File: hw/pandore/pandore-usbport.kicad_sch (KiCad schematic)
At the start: 12 parts, among them J2 USB2-A_2stacked, J3 USB3-A_2stacked

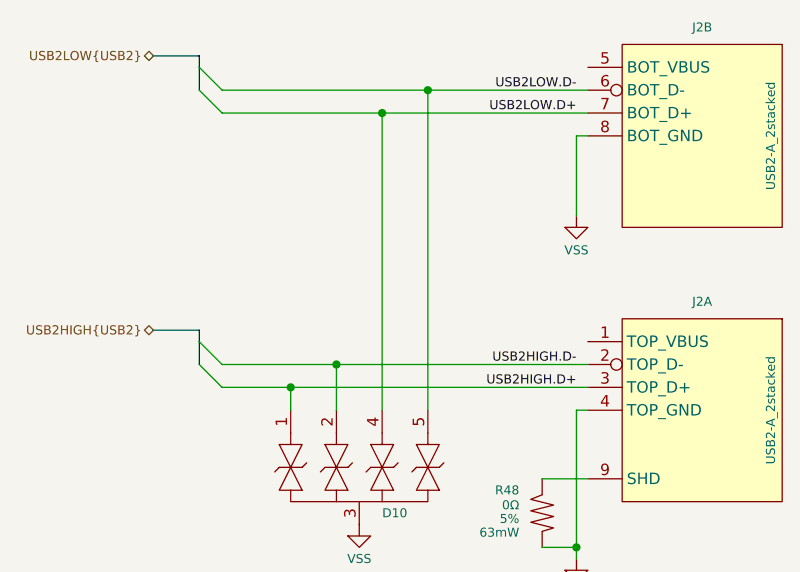
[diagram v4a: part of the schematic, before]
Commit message: added encoder, more routing done, pinout doc added
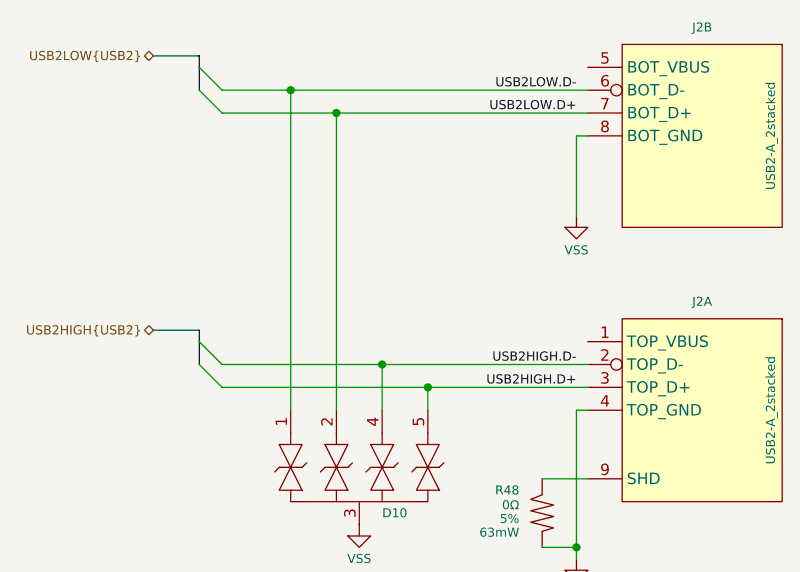
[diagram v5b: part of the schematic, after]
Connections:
- net USB2HIGH.D+: now also D10.5; no longer D10.1
- net USB2HIGH.D-: now also D10.4; no longer D10.2
- net USB2LOW.D+: now also D10.2; no longer D10.4
- net USB2LOW.D-: now also D10.1; no longer D10.5
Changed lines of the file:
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@@
-	)
-	(junction
-		(at 226.06 52.07)
-		(diameter 0)
-		(color 0 0 0 0)
 	)
 	(junction
@@
 	)
 	(junction
-		(at 231.14 24.13)
+		(at 226.06 24.13)
 		(diameter 0)
 		(color 0 0 0 0)
@@
 	)
 	(junction
+		(at 231.14 52.07)
+		(diameter 0)
+		(color 0 0 0 0)
+	)
+	(junction
 		(at 218.44 113.03)
 		(diameter 0)
@@
 	)
 	(junction
+		(at 220.98 21.59)
+		(diameter 0)
+		(color 0 0 0 0)
+	)
+	(junction
 		(at 223.52 110.49)
 		(diameter 0)
@@
 	)
 	(junction
+		(at 236.22 54.61)
+		(diameter 0)
+		(color 0 0 0 0)
+	)
+	(junction
 		(at 222.25 160.02)
 		(diameter 0)
@@
 	)
 	(junction
-		(at 236.22 21.59)
-		(diameter 0)
-		(color 0 0 0 0)
-	)
-	(junction
-		(at 220.98 54.61)
-		(diameter 0)
-		(color 0 0 0 0)
-	)
-	(junction
 		(at 210.82 95.25)
 		(diameter 0)
@@
 	(wire
 		(pts
+			(xy 231.14 52.07) (xy 231.14 57.15)
+		)
+		(stroke
+			(width 0)
+			(type default)
+		)
+	)
+	(wire
+		(pts
+			(xy 236.22 54.61) (xy 236.22 57.15)
+		)
+		(stroke
+			(width 0)
+			(type default)
+		)
+	)
+	(wire
+		(pts
 			(xy 176.53 110.49) (xy 190.5 110.49)
 		)
@@
 	(wire
 		(pts
-			(xy 213.36 54.61) (xy 220.98 54.61)
+			(xy 213.36 54.61) (xy 236.22 54.61)
 		)
 		(stroke
@@
 	(wire
 		(pts
+			(xy 226.06 24.13) (xy 254 24.13)
+		)
+		(stroke
+			(width 0)
+			(type default)
+		)
+	)
+	(wire
+		(pts
+			(xy 231.14 52.07) (xy 254 52.07)
+		)
+		(stroke
+			(width 0)
+			(type default)
+		)
+	)
+	(wire
+		(pts
 			(xy 248.92 64.77) (xy 254 64.77)
 		)
@@
 	(wire
 		(pts
-			(xy 220.98 54.61) (xy 254 54.61)
-		)
-		(stroke
-			(width 0)
-			(type default)
-		)
-	)
-	(wire
-		(pts
 			(xy 176.53 160.02) (xy 190.5 160.02)
 		)
@@
 	(wire
 		(pts
-			(xy 226.06 52.07) (xy 254 52.07)
-		)
-		(stroke
-			(width 0)
-			(type default)
-		)
-	)
-	(wire
-		(pts
-			(xy 236.22 21.59) (xy 236.22 57.15)
+			(xy 213.36 52.07) (xy 231.14 52.07)
 		)
 		(stroke
@@
 	(wire
 		(pts
-			(xy 213.36 21.59) (xy 236.22 21.59)
+			(xy 213.36 21.59) (xy 220.98 21.59)
 		)
 		(stroke
@@
 	(wire
 		(pts
-			(xy 213.36 52.07) (xy 226.06 52.07)
-		)
-		(stroke
-			(width 0)
-			(type default)
-		)
-	)
-	(wire
-		(pts
 			(xy 232.41 152.4) (xy 232.41 165.1)
 		)
@@
 	(wire
 		(pts
-			(xy 231.14 24.13) (xy 231.14 57.15)
-		)
-		(stroke
-			(width 0)
-			(type default)
-		)
-	)
-	(wire
-		(pts
 			(xy 227.33 154.94) (xy 254 154.94)
 		)
@@
 	(wire
 		(pts
+			(xy 236.22 54.61) (xy 254 54.61)
+		)
+		(stroke
+			(width 0)
+			(type default)
+		)
+	)
+	(wire
+		(pts
 			(xy 252.73 72.39) (xy 252.73 57.15)
 		)
@@
 	(wire
 		(pts
-			(xy 231.14 24.13) (xy 254 24.13)
-		)
-		(stroke
-			(width 0)
-			(type default)
-		)
-	)
-	(wire
-		(pts
 			(xy 254 97.79) (xy 252.73 97.79)
 		)
@@
 		)
 	)
-	(wire
-		(pts
-			(xy 220.98 54.61) (xy 220.98 57.15)
-		)
-		(stroke
-			(width 0)
-			(type default)
-		)
-	)
 	(bus
 		(pts
@@
 		)
 	)
+	(wire
+		(pts
+			(xy 220.98 21.59) (xy 220.98 57.15)
+		)
+		(stroke
+			(width 0)
+			(type default)
+		)
+	)
 	(bus
 		(pts
@@
 	(wire
 		(pts
+			(xy 226.06 24.13) (xy 226.06 57.15)
+		)
+		(stroke
+			(width 0)
+			(type default)
+		)
+	)
+	(wire
+		(pts
 			(xy 252.73 57.15) (xy 254 57.15)
 		)
@@
 	(wire
 		(pts
-			(xy 226.06 52.07) (xy 226.06 57.15)
-		)
-		(stroke
-			(width 0)
-			(type default)
-		)
-	)
-	(wire
-		(pts
 			(xy 176.53 92.71) (xy 208.28 92.71)
 		)
@@
 	(wire
 		(pts
-			(xy 236.22 21.59) (xy 254 21.59)
+			(xy 220.98 21.59) (xy 254 21.59)
 		)
 		(stroke
@@
 	(wire
 		(pts
-			(xy 213.36 24.13) (xy 231.14 24.13)
-		)
-		(stroke
+			(xy 213.36 24.13) (xy 226.06 24.13)
+		)
+		(stroke

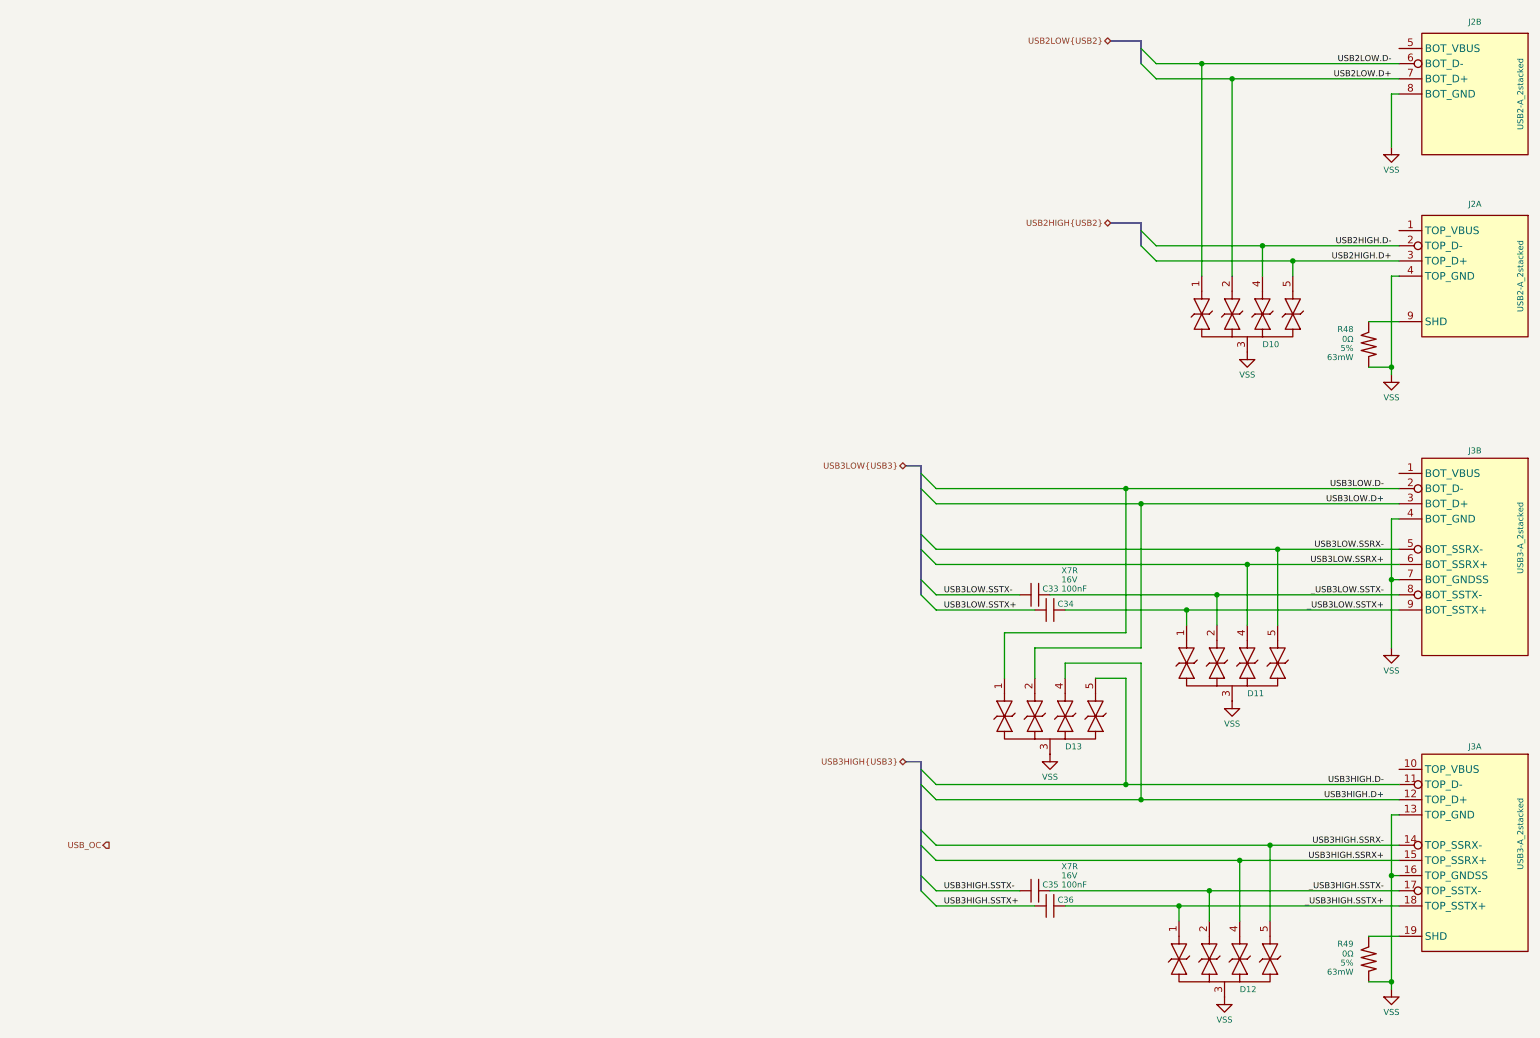
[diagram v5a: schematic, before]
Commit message: lcd control circuit added fan interface added rgba output pinout for management mcu accessories done
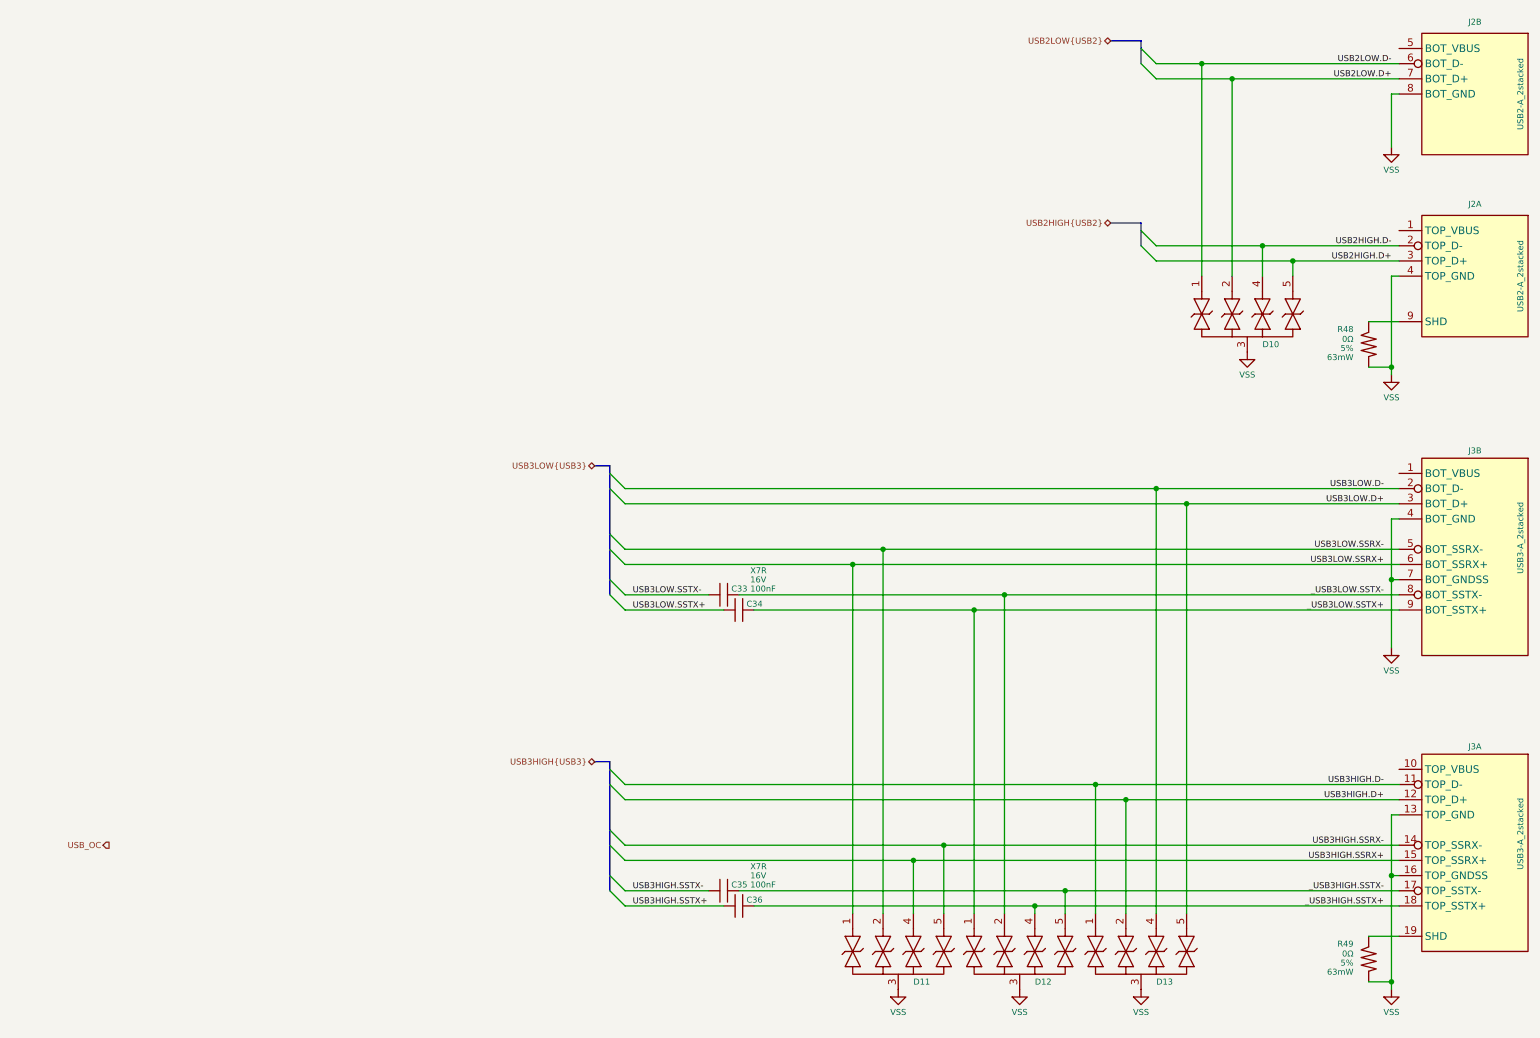
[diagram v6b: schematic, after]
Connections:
- net USB3HIGH.D+: now also D13.2; no longer D13.4
- net USB3HIGH.D-: now also D13.1; no longer D13.5
- net USB3HIGH.SSRX+: now also D11.4; no longer D12.4
- net USB3HIGH.SSRX-: now also D11.5; no longer D12.5
- net USB3LOW.D+: now also D13.5; no longer D13.2
- net USB3LOW.D-: now also D13.4; no longer D13.1
- net USB3LOW.SSRX+: now also D11.1; no longer D11.4
- net USB3LOW.SSRX-: now also D11.2; no longer D11.5
- net _USB3HIGH.SSTX+: now also D12.4; no longer D12.1
- net _USB3HIGH.SSTX-: now also D12.5; no longer D12.2
- net _USB3LOW.SSTX+: now also D12.1; no longer D11.1
- net _USB3LOW.SSTX-: now also D12.2; no longer D11.2
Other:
- moved on the sheet: C33, C34, C35, C36, D11, D12, D13

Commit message: more routing/placement done added 5v load switch 1A each added second fan circuit redone all diffpair routing following new stackup calc added all (?) missing connectors to unused pins
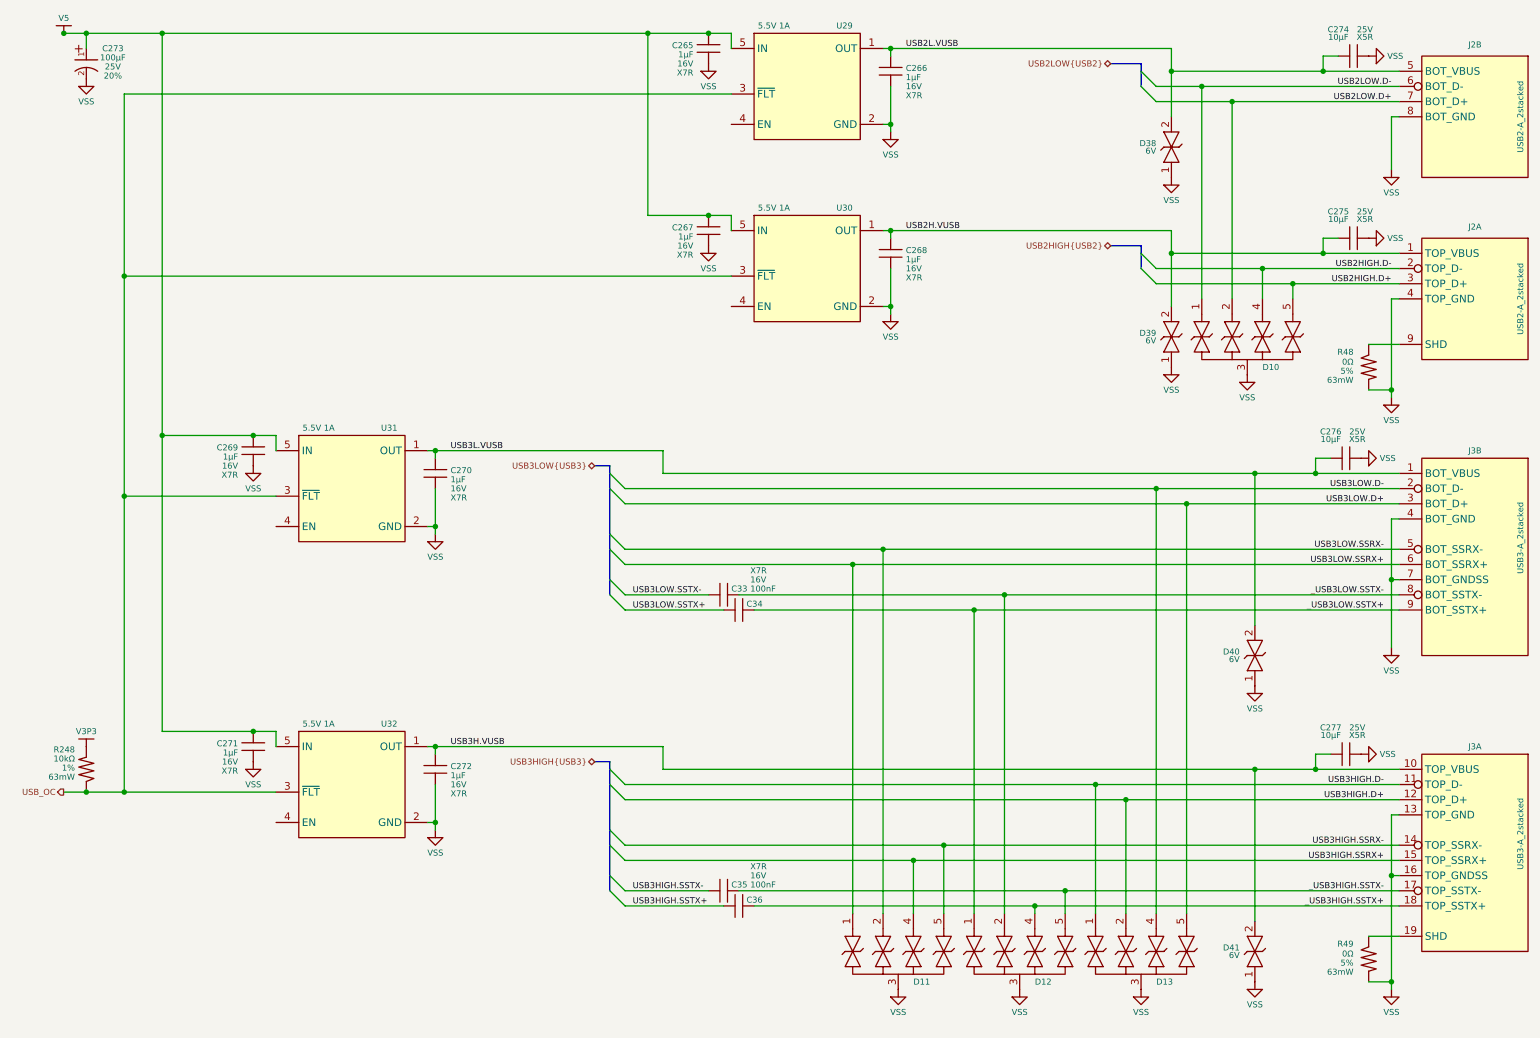
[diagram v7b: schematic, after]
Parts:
- added C265, C266, C267, C268, C269, C270, C271, C272: ${Capacitance}, ${Voltage}, ${Dielectric}, reekilib_cap:CAPC1608, symbol reekilib_cap:cap
- added C273: ${Capacitance}, ${Voltage}, ${Tolerance}, reekilib_cap:CAPAE630Xxxx, symbol reekilib_cap:cap_pol
- added C274, C275, C276, C277: ${Capacitance}, ${Voltage}, ${Dielectric}, reekilib_cap:CAPC2012, symbol reekilib_cap:cap
- added D38, D39, D40, D41: 6V, reekilib_dio:dio_sma, symbol reekilib_tvs:diode_tvsbi
- added R248: ${Resistance}, ${Tolerance}, ${Power}, reekilib_res:RESC1005, symbol reekilib_res:res
- added U29, U30, U31, U32: 5.5V 1A, reekilib_sot:SOT95P280X100-5, symbol reekilib_psw:ET2016x
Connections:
- net USB_OC: now also R248.2, U29.3 (~{FLT}), U30.3 (~{FLT}), U31.3 (~{FLT}), U32.3 (~{FLT})
- net VSS: now also C265.1, C266.1, C267.1, C268.1, C269.1, C270.1, C271.1, C272.1, C273.2 (-), C274.1, C275.1, C276.1, C277.1, D38.1, D39.1, D40.1, D41.1, U29.2 (GND), U30.2 (GND), U31.2 (GND), U32.2 (GND)
- net USB3L.VUSB: now reaches J3.1 (BOT_VBUS)
- net USB3L.VUSB: now also C270.2, C276.2, D40.2, U31.1 (OUT)
- net USB2L.VUSB: now reaches J2.5 (BOT_VBUS)
- net USB2L.VUSB: now also C266.2, C274.2, D38.2, U29.1 (OUT)
- net USB2H.VUSB: now reaches J2.1 (TOP_VBUS)
- net USB2H.VUSB: now also C268.2, C275.2, D39.2, U30.1 (OUT)
- net USB3H.VUSB: now reaches J3.10 (TOP_VBUS)
- net USB3H.VUSB: now also C272.2, C277.2, D41.2, U32.1 (OUT)
- new net V3P3: R248.1
- new net V5: C265.2, C267.2, C269.2, C271.2, C273.1 (+), U29.5 (IN), U30.5 (IN), U31.5 (IN), U32.5 (IN)
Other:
- moved on the sheet: D10, J2A, J2B, R48

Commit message: all routed, review starting
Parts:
- added R63: ${Resistance}, ${Tolerance}, ${Power}, reekilib_res:RESC1005, symbol reekilib_res:res
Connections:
- net V3P3: now also R63.2
- net VUSB.EN: now reaches U30.4 (EN)
- net VUSB.EN: now also U29.4 (EN), U31.4 (EN), U32.4 (EN), R63.1
